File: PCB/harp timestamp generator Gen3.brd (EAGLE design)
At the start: 124.5 x 80.4 mm, 140 parts, among them IC1 SI8621BC-B-IS, IC10 SN74LVC1G125DBVT, IC11 SI8621BC-B-IS, IC12 SI8621BC-B-IS, IC13 SI8621BC-B-IS, IC14 SI8621BC-B-IS, IC15 ATXMEGAxxxA4U-AU, IC2 USBLC6-2SC6, IC3 FT232RL, IC4 TLV70033DDCR, IC5 TLV70033DDCR, IC6 SI8621BC-B-IS, IC8 SN74LVC1G125DBVT, IC9 SN74LVC1G125DBVT, Q1 RTU002P02T106, Q2 BC817-40W, Q3 BC817-40LT1SMD, Q6 DMP2035U-7, T10 BC850, T11 BC850, T12 BC850, T13 BC850, T4 BC850, T5 BC850, T6 BC850, T7 BC850, T8 BC850, T9 BC850, U1 MCP73831T-2ATI/OT, U2 ICL7673CBAZA-T, X1 B2B-PH-K-S(LF)(SN)

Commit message: Corrected buffers' enable.
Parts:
- removed T11, T12, T13: BC850, transistor:SOT23
- removed U1: MCP73831T-2ATI/OT, harp timestamp generator:TSOT23-5
- removed U2: ICL7673CBAZA-T, harp timestamp generator:SOIC8
- added IC17: SI8621BC-B-IS, harp timestamp generator:SOIC8
- added IC19: SN74LVC1G125DBVT, 74xx-little-de:SOT23-5
- added T1, T2, T3: BC850, transistor:SOT23
- IC1: value SI8621BC-B-IS -> MCP73831T-2ATI/OT; device harp timestamp generator:SOIC8 -> harp timestamp generator:TSOT23-5
- IC11: value SI8621BC-B-IS -> TLV70033DDCR; device harp timestamp generator:SOIC8 -> harp timestamp generator:TSOT23-5
- IC15: value ATXMEGAxxxA4U-AU -> SI8621BC-B-IS; device harp timestamp generator:QFP80P1200X1200X120-44N -> harp timestamp generator:SOIC8
- IC16: value (none) -> SI8621BC-B-IS; device 74xx-little-de:SC70-5 -> harp timestamp generator:SOIC8
- IC18: value (none) -> SN74LVC1G125DBVT; device 74xx-little-de:SC70-5 -> 74xx-little-de:SOT23-5
- IC4: value TLV70033DDCR -> ICL7673CBAZA-T; device harp timestamp generator:TSOT23-5 -> harp timestamp generator:SOIC8
- IC6: value SI8621BC-B-IS -> ATXMEGAxxxA4U-AU; device harp timestamp generator:SOIC8 -> harp timestamp generator:QFP80P1200X1200X120-44N
- IC7: value (none) -> M74VHC1GT126DF1G
- IC8, IC9: value SN74LVC1G125DBVT -> M74VHC1GT126DF1G; device 74xx-little-de:SOT23-5 -> 74xx-little-de:SC70-5
- moved IC11 50.5 mm to (98.9, 72.3), turned to 90 degrees
- moved IC6 44.0 mm to (44.0, 28.0), turned to 90 degrees
- moved IC16 40.6 mm to (25.0, 59.0), turned to 0 degrees
- moved IC1 38.4 mm to (98.0, 44.0), turned to 90 degrees
- moved IC12 37.6 mm to (75.2, 59.0)
- moved IC13 37.6 mm to (62.6, 59.0)
- moved IC14 37.6 mm to (50.2, 59.0)
- moved IC9 33.0 mm to (43.0, 12.5), turned to 270 degrees
- moved IC18 33.0 mm to (47.0, 45.2), turned to 0 degrees
- moved IC8 32.8 mm to (28.0, 18.5), turned to 270 degrees
- moved IC15 31.7 mm to (37.6, 59.0), turned to 0 degrees
- moved IC4 23.2 mm to (76.0, 45.0), turned to 180 degrees
- moved IC5 13.0 mm to (93.0, 60.8)
- moved T8 12.3 mm to (111.8, 20.7)
- moved T7 12.3 mm to (107.7, 20.7)
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- renumbered Q6 to Q5, TEST to BUTTON
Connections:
- net +3V3: now also IC15.1, IC16.1, IC17.1, IC18.5, IC19.5, IC5.5; no longer IC1.1, IC11.1, IC4.5, IC6.1, IC8.5, IC9.5
- net +5V: now also IC11.1, IC11.3, IC7.1, IC8.1, IC8.5, IC9.1, IC9.5; no longer IC16.5, IC18.5, IC4.3, U2.1
- net +5_USB: now also IC4.8; no longer U2.8
- net BAT_READ: now also IC6.41; no longer IC15.41
- net BAT_VOLTAGE: now also IC6.40; no longer IC15.40
- net BLIGHT_EN_UC: now also IC6.1, IC8.2; no longer IC15.1, IC16.2
- net BUTTON: now also IC6.7; no longer IC15.7
- net CHARGE_ENABLE: now also IC6.5; no longer IC15.5
- net CLKOUT0: now also IC12.7; no longer IC6.7
- net CLKOUT1: now also IC13.7; no longer IC1.7
- net CLKOUT2: now also IC14.7; no longer IC11.7
- net CLKOUT3: now also IC15.7; no longer IC12.7
- net CLKOUT4: now also IC16.7; no longer IC13.7
- net CLKOUT5: now also IC17.7; no longer IC14.7
- net CLOCK_IN: now also IC18.2, IC6.26; no longer IC15.26, IC8.2
- net CLOCK_OUT: now also IC19.2, IC6.27; no longer IC15.27, IC9.2
- net CLOCK_OUT_ISO: now also IC15.2, IC16.2, IC17.2, IC18.4, IC19.4; no longer IC1.2, IC11.2, IC6.2, IC8.4, IC9.4
- net DEVICE_AT_0: now also IC12.3, IC6.16; no longer IC15.16, IC6.3
- net DEVICE_AT_1: now also IC13.3, IC6.17; no longer IC1.3, IC15.17
- net DEVICE_AT_2: now also IC14.3, IC6.44; no longer IC11.3, IC15.44
- net DEVICE_AT_3: now also IC15.3, IC6.36; no longer IC12.3, IC15.36
- net DEVICE_AT_4: now also IC16.3, IC6.42; no longer IC13.3, IC15.42
- net DEVICE_AT_5: now also IC17.3, IC6.43; no longer IC14.3, IC15.43
- net DISCHARGE_BAT: now also IC6.6; no longer IC15.6
- net EN_CLOCK_IN: now also IC18.1, IC6.22; no longer IC15.22, IC8.1
- net EN_CLOCK_OUT: now also IC19.1, IC6.21; no longer IC15.21, IC9.1
- net FTDI_CTS: now also IC6.29; no longer IC15.29
- net FTDI_RTS: now also IC6.28; no longer IC15.28
- net FTDI_RXD: now also IC6.33; no longer IC15.33
- net FTDI_TXD: now also IC6.32; no longer IC15.32
- net GND: now also IC1.2, IC11.2, IC15.4, IC16.4, IC17.4, IC19.3, IC4.4, IC6.18, IC6.30, IC6.38, IC6.8, T1.2, T2.2, T3.2; no longer IC1.4, IC11.4, IC15.18, IC15.30, IC15.38, IC15.8, IC16.3, IC4.2, IC6.4, T11.2, T12.2, T13.2, U1.2, U2.4
- net GND_ISO: now also IC12.5; no longer IC6.5
- net GND_ISO1: now also IC13.5; no longer IC1.5
- net GND_ISO2: now also IC14.5; no longer IC11.5
- net GND_ISO3: now also IC15.5; no longer IC12.5
- net GND_ISO4: now also IC16.5; no longer IC13.5
- net GND_ISO5: now also IC17.5; no longer IC14.5
- net LED_CLK_0: now also IC6.10; no longer IC15.10
- net LED_CLK_1: now also IC6.11; no longer IC15.11
- net LED_CLK_2: now also IC6.12; no longer IC15.12
- net LED_CLK_3: now also IC6.13; no longer IC15.13
- net LED_CLK_4: now also IC6.14; no longer IC15.14
- net LED_CLK_5: now also IC6.15; no longer IC15.15
- net LED_LOCK: now also IC6.24; no longer IC15.24
- net LED_PWR: now also IC6.20; no longer IC15.20
- net LED_REP: now also IC6.23; no longer IC15.23
- net N$1: now also T7.1; no longer T10.1
- net N$10: now also IC1.4; no longer U1.4
- net N$11: now also IC14.6, IC14.8; no longer IC11.6, IC11.8
- net N$15: now also T3.1; no longer T6.1
- net N$16: now also IC1.5; no longer U1.5
- net N$17: now also T1.1; no longer T4.1
- net N$19: now also T1.3; no longer T4.3
- net N$20: now also T2.1; no longer T5.1
- net N$21: now also T3.3; no longer T6.3
- net N$22: now also T2.3; no longer T5.3
- net N$24: now also T4.1; no longer T7.1
- net N$25: now also T4.3; no longer T7.3
- net N$26: now also T5.1; no longer T8.1
- net N$27: now also T5.3; no longer T8.3
- net N$28: now also T6.1; no longer T9.1
- net N$29: now also T6.3; no longer T9.3
- net N$3: now also IC8.4; no longer IC16.4
- net N$34: now also T8.1; no longer T11.1
- net N$37: now also IC15.6, IC15.8; no longer IC12.6, IC12.8
- net N$4: now also IC9.4; no longer IC18.4
- net N$42: now also IC11.5; no longer IC5.5
- net N$45: now also IC16.6, IC16.8; no longer IC13.6, IC13.8
- net N$47: now also T8.3; no longer T11.3
- net N$49: now also IC17.6, IC17.8; no longer IC14.6, IC14.8
- net N$5: now also IC12.6, IC12.8; no longer IC6.6, IC6.8
- net N$53: now also T9.1; no longer T12.1
- net N$54: now also T9.3; no longer T12.3
- net N$56: now also T10.1; no longer T13.1
- net N$6: now also IC13.6, IC13.8; no longer IC1.6, IC1.8
- net N$60: now also T10.3; no longer T13.3
- net N$7: now also T7.3; no longer T10.3
- net N$97: now also IC1.3; no longer U1.3
- net OSC1: now also IC6.37; no longer IC15.37
- net PDI-CLK: now also IC6.35; no longer IC15.35
- net PDI-DATA: now also IC6.34; no longer IC15.34
- net PWR_GOOD: now also IC4.6, IC6.4; no longer IC15.4, U2.6
- net STATE: now also IC6.25; no longer IC15.25
- net UC_RX: now also IC6.2; no longer IC15.2
- net UC_TX: now also IC6.3, IC9.2; no longer IC15.3, IC18.2
- net VDD: now also IC6.19, IC6.31, IC6.39, IC6.9; no longer IC15.19, IC15.31, IC15.39, IC15.9
- net V_BATT: now also IC4.2; no longer U2.2
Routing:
- net +3V3: track 357.1 -> 353.8 mm, vias 20 -> 19
- net IDC_CLOCK_OUT: track 41.2 -> 37.9 mm
- net BLIGHT_EN: track 8.38 -> 5.21 mm
- net TX: track 25.6 -> 23.0 mm
- net RX: track 22.4 -> 19.8 mm
- net V_BATT: track 63.6 -> 61.0 mm
- net +5V: track 202.0 -> 204.5 mm
- net +5_USB: track 56.7 -> 56.1 mm, vias 3 -> 5
- net GND: vias 222 -> 226
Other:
- board text added: "For Research Use Only"
- board text added: "harp timsestamp generator Gen3 v1.0"
- board text removed: "FILIPE: foram feitas alguns add-ons não envies para produção antes de falarmos levantaramse-me algumas questões que devemos falar"
- board text removed: "harp timsestamp generator v1.0"

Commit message: Big updates. Very close to final design.
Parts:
- C33: value 4.7n -> 10n
- F1: value 10MHz ?? -> 330 Ohms @ 100MHz
- IC6: value ATXMEGAxxxA4U-AU -> ATXMEGA16A4U-AU
- PDI: value (none) -> 2x3_header
- Q4: value (none) -> DMG1012UW
- R14: value 10k ?? -> 10k
- R5: value 15K 0.1% -> 15K 0.1% => 14k7

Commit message: Increased battery current draw to around 250 mA.
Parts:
- R15: value 25R -> 15R
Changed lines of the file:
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@@
 <?xml version="1.0" encoding="utf-8"?>
 <!DOCTYPE eagle SYSTEM "eagle.dtd">
-<eagle version="9.6.2">
+<eagle version="9.5.1">
 <drawing>
 <settings>
@@
 <attribute name="DIGKEYPN" value="ATXMEGA16A4U-AU-ND" x="44" y="28" size="1.778" layer="27" rot="R90" display="off"/>
 <attribute name="MPN" value="ATXMEGA16A4U-AU" x="44" y="28" size="1.778" layer="27" rot="R90" display="off"/>
+<attribute name="NAME" x="38.2" y="36" size="0.8128" layer="51" font="vector" ratio="15" rot="R180" display="off"/>
 <attribute name="NAME" x="38.9" y="22.2" size="0.8128" layer="21" font="vector" ratio="15" rot="R180"/>
-<attribute name="NAME" x="38.2" y="36" size="0.8128" layer="51" font="vector" ratio="15" rot="R180" display="off"/>
 <attribute name="VALUE" x="49.2" y="36" size="0.7" layer="21" ratio="5" rot="R180"/>
 </element>
@@
 <attribute name="VALUE" x="63.905" y="35.365" size="1.27" layer="27" rot="R90"/>
 </element>
-<element name="R15" library="rcl" package="R2512" value="25R" x="75" y="35.6" smashed="yes" rot="R180">
+<element name="R15" library="rcl" package="R2512" value="15R" x="75" y="35.6" smashed="yes" rot="R180">
 <attribute name="DIGKEYPN" value="541-2662-1-ND" x="75" y="35.6" size="1.778" layer="27" rot="R180" display="off"/>
 <attribute name="MPN" value="RCP2512W25R0GEB" x="75" y="35.6" size="1.778" layer="27" rot="R180" display="off"/>

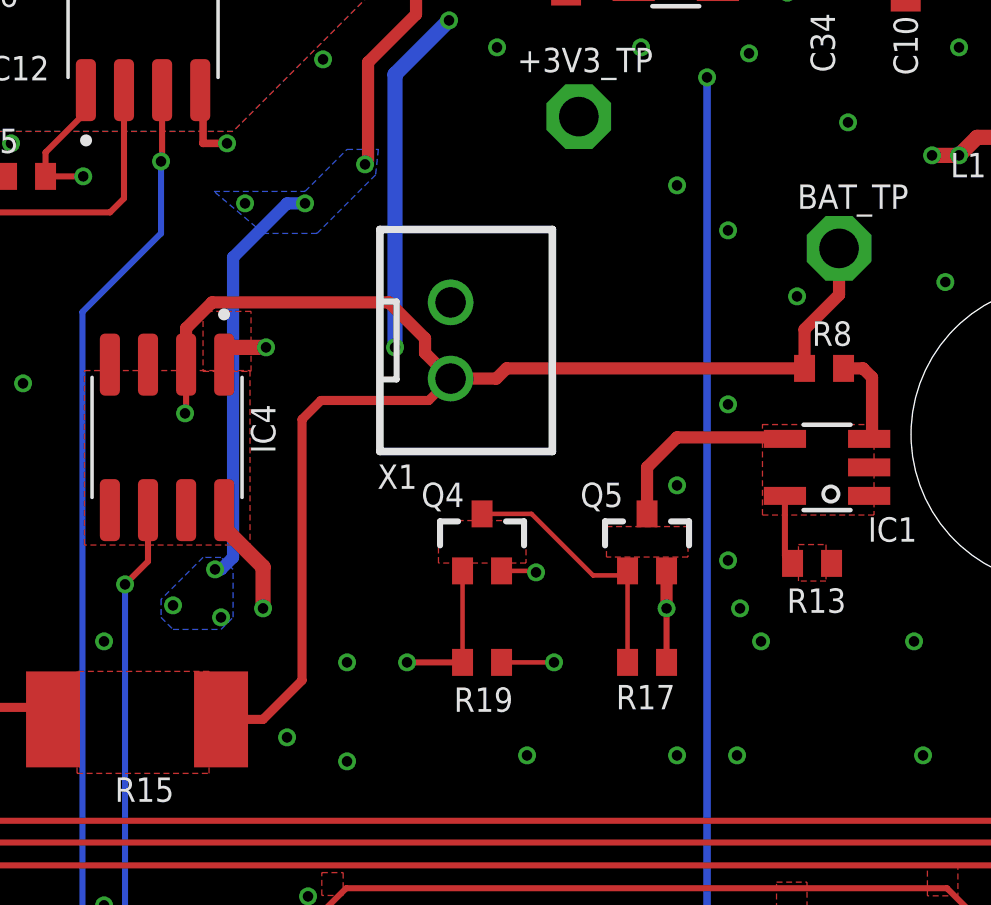
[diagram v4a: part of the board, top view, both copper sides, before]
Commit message: Corrected X1 PN and PCB's orientation.
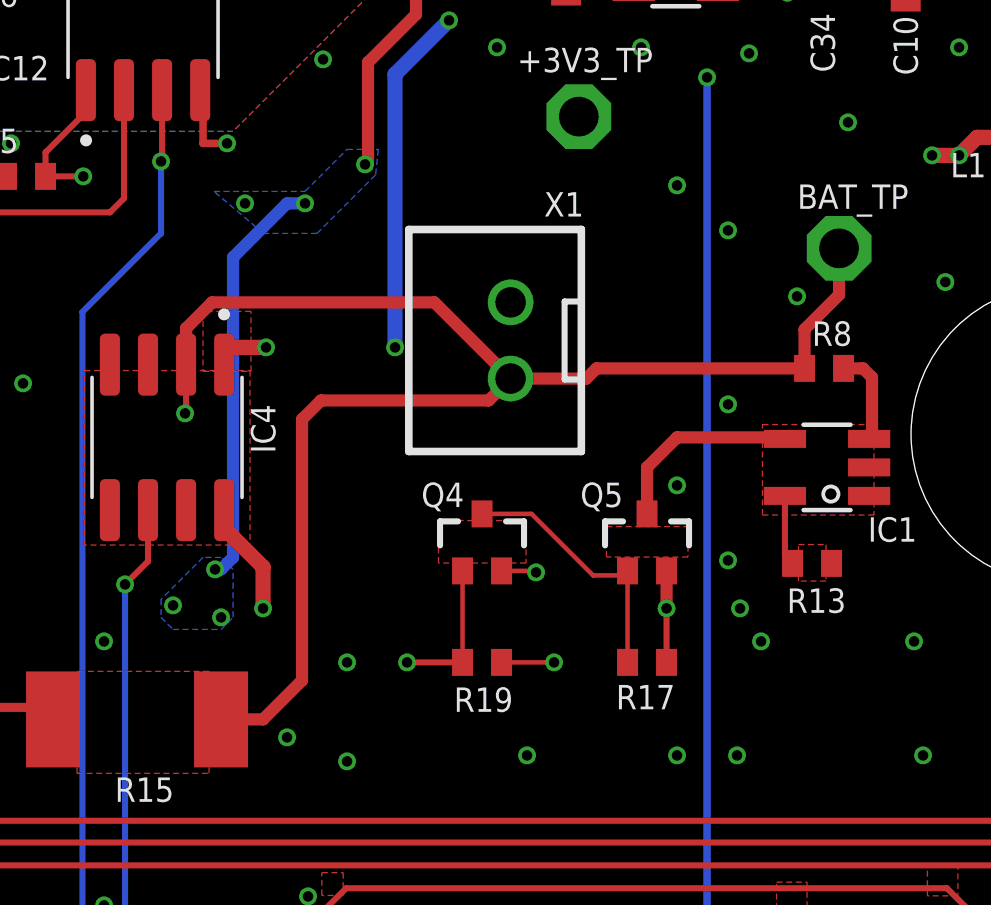
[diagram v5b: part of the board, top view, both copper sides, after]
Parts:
- moved X1 2.00 mm to (87.5, 48.2), turned to 90 degrees
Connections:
- net GND: now also X1.2; no longer X1.1
- net V_BATT: now also X1.1; no longer X1.2
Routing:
- net V_BATT: track 61.0 -> 62.7 mm
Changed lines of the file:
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@@
 <setting verticaltext="up"/>
 </settings>
-<grid distance="10" unitdist="mil" unit="mm" style="dots" multiple="1" display="yes" altdistance="0.1" altunitdist="mm" altunit="mm"/>
+<grid distance="8" unitdist="mil" unit="mil" style="dots" multiple="1" display="yes" altdistance="0.1" altunitdist="mm" altunit="mm"/>
 <layers>
 <layer number="1" name="Top" color="4" fill="1" visible="yes" active="yes"/>
@@
 <attribute name="DIGKEYPN" value="ATXMEGA16A4U-AU-ND" x="44" y="28" size="1.778" layer="27" rot="R90" display="off"/>
 <attribute name="MPN" value="ATXMEGA16A4U-AU" x="44" y="28" size="1.778" layer="27" rot="R90" display="off"/>
-<attribute name="NAME" x="38.2" y="36" size="0.8128" layer="51" font="vector" ratio="15" rot="R180" display="off"/>
 <attribute name="NAME" x="38.9" y="22.2" size="0.8128" layer="21" font="vector" ratio="15" rot="R180"/>
+<attribute name="NAME" x="38.2" y="36" size="0.8128" layer="51" font="vector" ratio="15" rot="R180" display="off"/>
 <attribute name="VALUE" x="49.2" y="36" size="0.7" layer="21" ratio="5" rot="R180"/>
 </element>
@@
 <attribute name="VALUE" x="30.135" y="51.005" size="1.27" layer="27" rot="R180"/>
 </element>
-<element name="X1" library="harp timestamp generator" package="JST-XH-02-PACKAGE-ROUND-PAD" value="B2B-PH-K-S(LF)(SN)" x="85.452" y="48.23" smashed="yes" rot="R270">
-<attribute name="DIGKEYPN" value="455-1704-ND" x="85.452" y="48.23" size="1.778" layer="27" rot="R270" display="off"/>
-<attribute name="MPN" value="B2B-PH-K-S(LF)(SN)" x="85.452" y="48.23" size="1.778" layer="27" rot="R270" display="off"/>
-<attribute name="NAME" x="83.012" y="43.285" size="0.8128" layer="25" font="vector" ratio="15"/>
-<attribute name="VALUE" x="89.3445" y="51.5325" size="1.016" layer="27" ratio="10" rot="R270"/>
+<element name="X1" library="harp timestamp generator" package="JST-XH-02-PACKAGE-ROUND-PAD" value="B2B-PH-K-S(LF)(SN)" x="87.452" y="48.23" smashed="yes" rot="R90">
+<attribute name="DIGKEYPN" value="455-1704-ND" x="87.452" y="48.23" size="1.778" layer="27" rot="R90" display="off"/>
+<attribute name="MPN" value="B2B-PH-K-S(LF)(SN)" x="87.452" y="48.23" size="1.778" layer="27" rot="R90" display="off"/>
+<attribute name="NAME" x="89.892" y="53.175" size="0.8128" layer="25" font="vector" ratio="15" rot="R180"/>
+<attribute name="VALUE" x="83.5595" y="44.9275" size="1.016" layer="27" ratio="10" rot="R90"/>
 </element>
 <element name="IC1" library="harp timestamp generator" package="TSOT23-5" value="MCP73831T-2ATI/OT" x="98" y="44" smashed="yes" rot="R90">
@@
 <contactref element="IC7" pad="3"/>
 <contactref element="C37" pad="2"/>
-<contactref element="X1" pad="1"/>
 <contactref element="IC1" pad="2"/>
 <contactref element="R13" pad="1"/>
@@
 <via x="94.7" y="40.9" extent="1-16" drill="0.35"/>
 <via x="98.7" y="55.5" extent="1-16" drill="0.35"/>
+<contactref element="X1" pad="2"/>
 </signal>
 <signal name="CLOCK_IN">
@@
 </signal>
 <signal name="V_BATT">
-<contactref element="X1" pad="2"/>
 <contactref element="R7" pad="1"/>
 <contactref element="Q1" pad="1"/>
@@
 <contactref element="R15" pad="1"/>
 <wire x1="64.3" y1="46.35" x2="66.65" y2="46.35" width="0.2032" layer="1"/>
-<wire x1="97.25" y1="47.3" x2="87.316" y2="47.3" width="0.4064" layer="1"/>
-<wire x1="87.316" y1="47.3" x2="86.976" y2="46.96" width="0.4064" layer="1"/>
-<wire x1="86.976" y1="46.96" x2="85.452" y2="46.96" width="0.4064" layer="1"/>
-<wire x1="85.452" y1="46.96" x2="84.6" y2="47.812" width="0.4064" layer="1"/>
-<wire x1="84.6" y1="47.812" x2="84.6" y2="48.3" width="0.4064" layer="1"/>
-<wire x1="84.6" y1="48.3" x2="83.4" y2="49.5" width="0.4064" layer="1"/>
-<wire x1="77.5" y1="49.5" x2="76.635" y2="48.635" width="0.4064" layer="1"/>
+<wire x1="97.25" y1="47.3" x2="90.316" y2="47.3" width="0.4064" layer="1"/>
+<wire x1="76.635" y1="48.635" x2="77.5" y2="49.5" width="0.4064" layer="1"/>
 <wire x1="76.635" y1="48.635" x2="76.635" y2="47.425" width="0.4064" layer="1"/>
-<wire x1="83.4" y1="49.5" x2="77.5" y2="49.5" width="0.4064" layer="1"/>
-<wire x1="80.5" y1="36.9" x2="79.2" y2="35.6" width="0.3048" layer="1"/>
-<wire x1="77.8" y1="35.6" x2="79.2" y2="35.6" width="0.3048" layer="1"/>
-<wire x1="85.452" y1="46.96" x2="84.722" y2="46.23" width="0.3048" layer="1"/>
-<wire x1="84.722" y1="46.23" x2="81.13" y2="46.23" width="0.3048" layer="1"/>
-<wire x1="80.5" y1="36.9" x2="80.5" y2="45.6" width="0.3048" layer="1"/>
-<wire x1="80.5" y1="45.6" x2="81.13" y2="46.23" width="0.3048" layer="1"/>
+<wire x1="80.5" y1="36.9" x2="79.2" y2="35.6" width="0.4064" layer="1"/>
+<wire x1="77.8" y1="35.6" x2="79.2" y2="35.6" width="0.4064" layer="1"/>
+<wire x1="80.5" y1="36.9" x2="80.5" y2="45.6" width="0.4064" layer="1"/>
+<wire x1="80.5" y1="45.6" x2="81.13" y2="46.23" width="0.4064" layer="1"/>
 <wire x1="98.4" y1="51.3" x2="98.4" y2="49.75" width="0.4064" layer="1"/>
 <wire x1="98.4" y1="49.75" x2="97.25" y2="48.6" width="0.4064" layer="1"/>
@@
 <wire x1="66.6" y1="45.2" x2="66.6" y2="46.3" width="0.2032" layer="1"/>
 <wire x1="66.6" y1="46.3" x2="66.65" y2="46.35" width="0.2032" layer="1"/>
+<contactref element="X1" pad="1"/>
+<wire x1="86.722" y1="46.23" x2="87.452" y2="46.96" width="0.4064" layer="1"/>
+<wire x1="81.13" y1="46.23" x2="86.722" y2="46.23" width="0.4064" layer="1"/>
+<wire x1="90.316" y1="47.3" x2="89.976" y2="46.96" width="0.4064" layer="1"/>
+<wire x1="89.976" y1="46.96" x2="87.452" y2="46.96" width="0.4064" layer="1"/>
+<wire x1="84.912" y1="49.5" x2="87.452" y2="46.96" width="0.4064" layer="1"/>
+<wire x1="77.5" y1="49.5" x2="84.912" y2="49.5" width="0.4064" layer="1"/>
 </signal>
 <signal name="N$10">
